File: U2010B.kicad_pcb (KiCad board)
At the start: 2 copper layers, 27 parts, among them J1 PHASE, J2 M2, J3 Rsh, J4 Rsh, J5 NULL, J6 M1, P1 50k, Q1 BT136-600, U1 U2010B

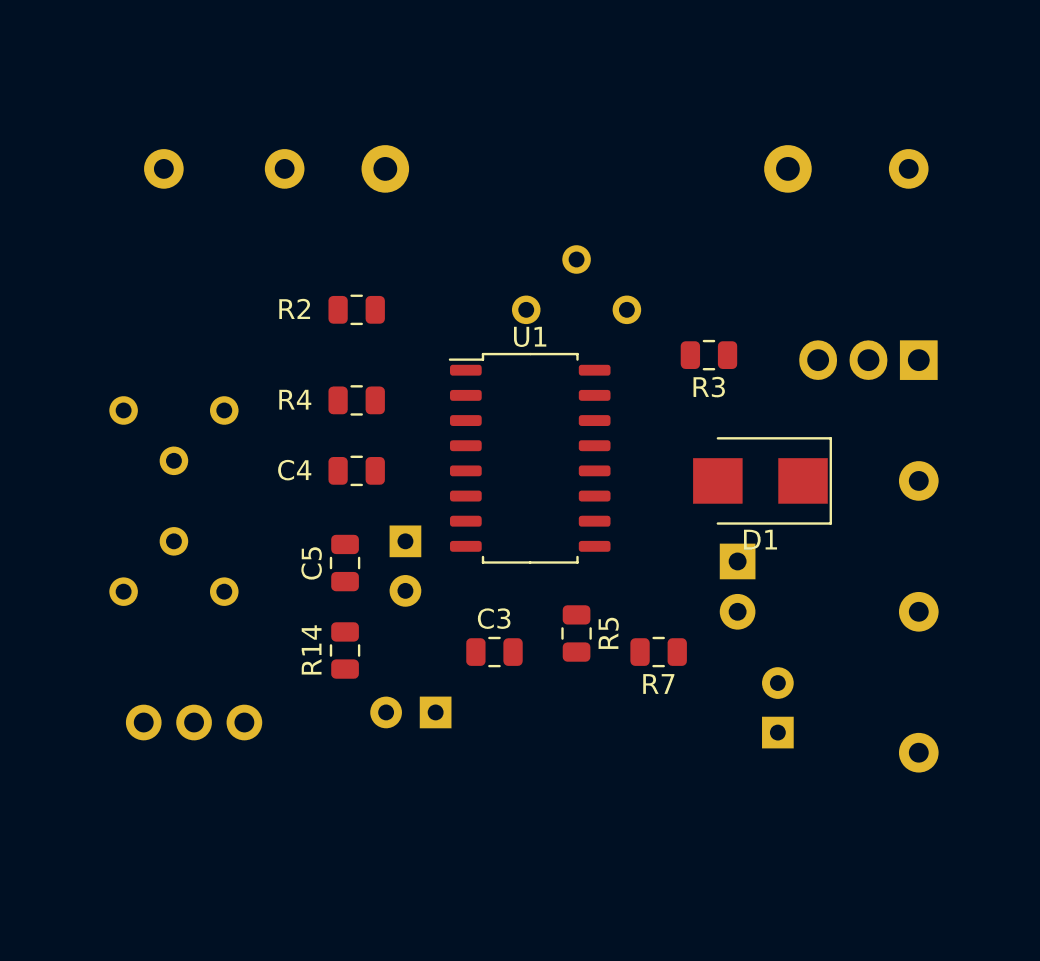
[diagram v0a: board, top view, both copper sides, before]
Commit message: Trace PCB
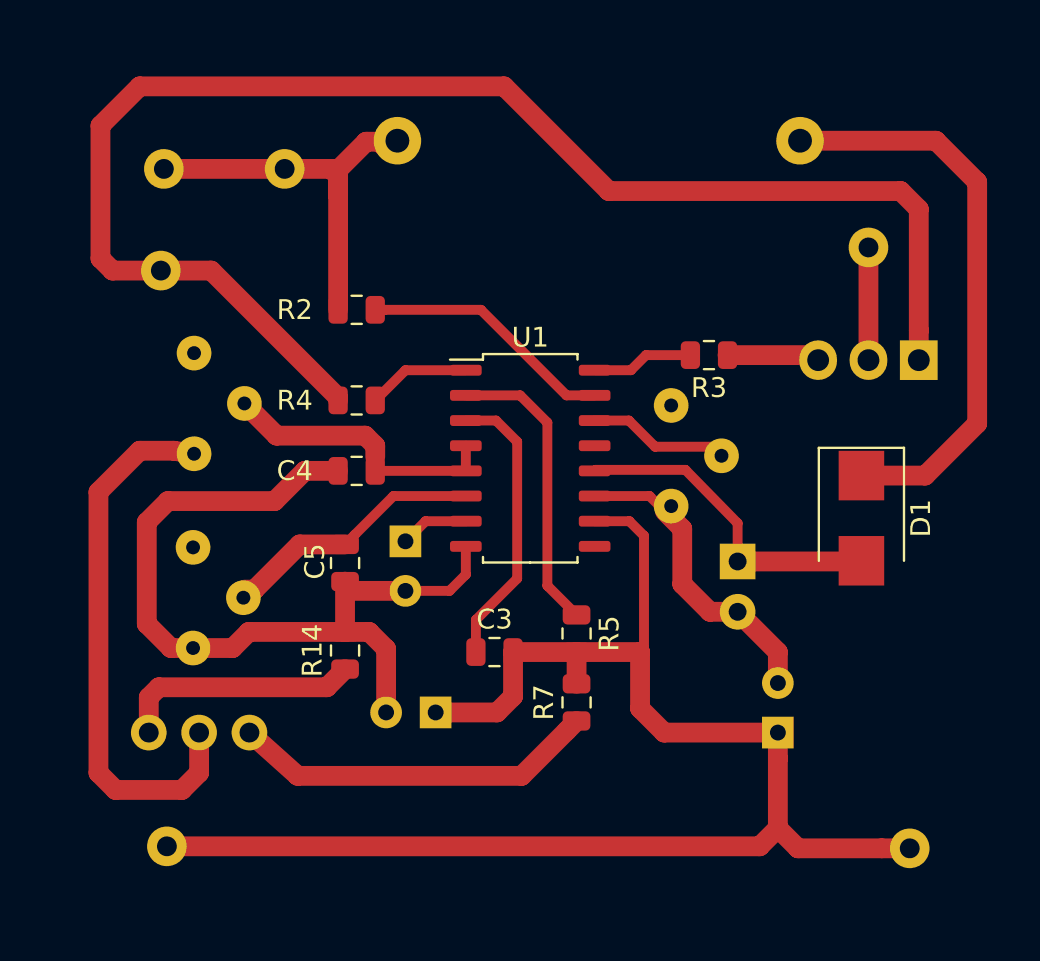
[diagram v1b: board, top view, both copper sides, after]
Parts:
- R10, R11, R8: footprint Potentiometer_THT:Potentiometer_Vishay_T7-YA_Single_Vertical -> Potentiometer_THT:Potentiometer_Bourns_3339P_Vertical_HandSoldering
- moved J3 39.7 mm to (121.3, 98.6)
- moved J4 38.2 mm to (121.6, 127.7)
- moved R8 12.3 mm to (147.0, 110.5), turned to 180 degrees
- moved J5 11.9 mm to (159.1, 127.8)
- moved D1 5.43 mm to (156.6, 111.1), turned to 270 degrees
- moved R7 4.86 mm to (142.2, 120.4), turned to 90 degrees
- moved R11 4.51 mm to (122.9, 117.7), turned to 180 degrees
- moved J6 4.45 mm to (157.0, 97.4)
- moved R10 2.66 mm to (122.9, 107.8), turned to 180 degrees
- moved R1 1.55 mm to (153.5, 92.0)
- moved P1 0.57 mm to (125.7, 121.9)
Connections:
- U1 pad 13: Net-(U1-Pad13) -> (no net)
- U1 pad 9: Net-(U1-Pad9) -> (no net)
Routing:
- net Net-(C1-Pad1): track 0.00 -> 76.7 mm
- net Net-(J3-Pad1): track 0.00 -> 74.1 mm
- net Net-(C2-Pad2): track 0.00 -> 42.2 mm
- net Net-(D1-Pad1): track 0.00 -> 28.9 mm
- net Net-(P1-Pad2): track 0.00 -> 27.7 mm
- net Net-(J1-Pad1): track 0.00 -> 20.1 mm
- net Net-(P1-Pad1): track 0.00 -> 18.5 mm
- net Net-(D1-Pad2): track 0.00 -> 16.6 mm
- net Net-(C1-Pad2): track 0.00 -> 16.1 mm
- net Net-(R5-Pad1): track 0.00 -> 15.0 mm
- net Net-(C4-Pad2): track 0.00 -> 14.6 mm
- net Net-(C3-Pad1): track 0.00 -> 14.5 mm
- net Net-(C5-Pad2): track 0.00 -> 13.1 mm
- net Net-(R2-Pad2): track 0.00 -> 12.9 mm
- net Net-(P1-Pad3): track 0.00 -> 12.3 mm
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
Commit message: Add netlist, change some pins for drill.
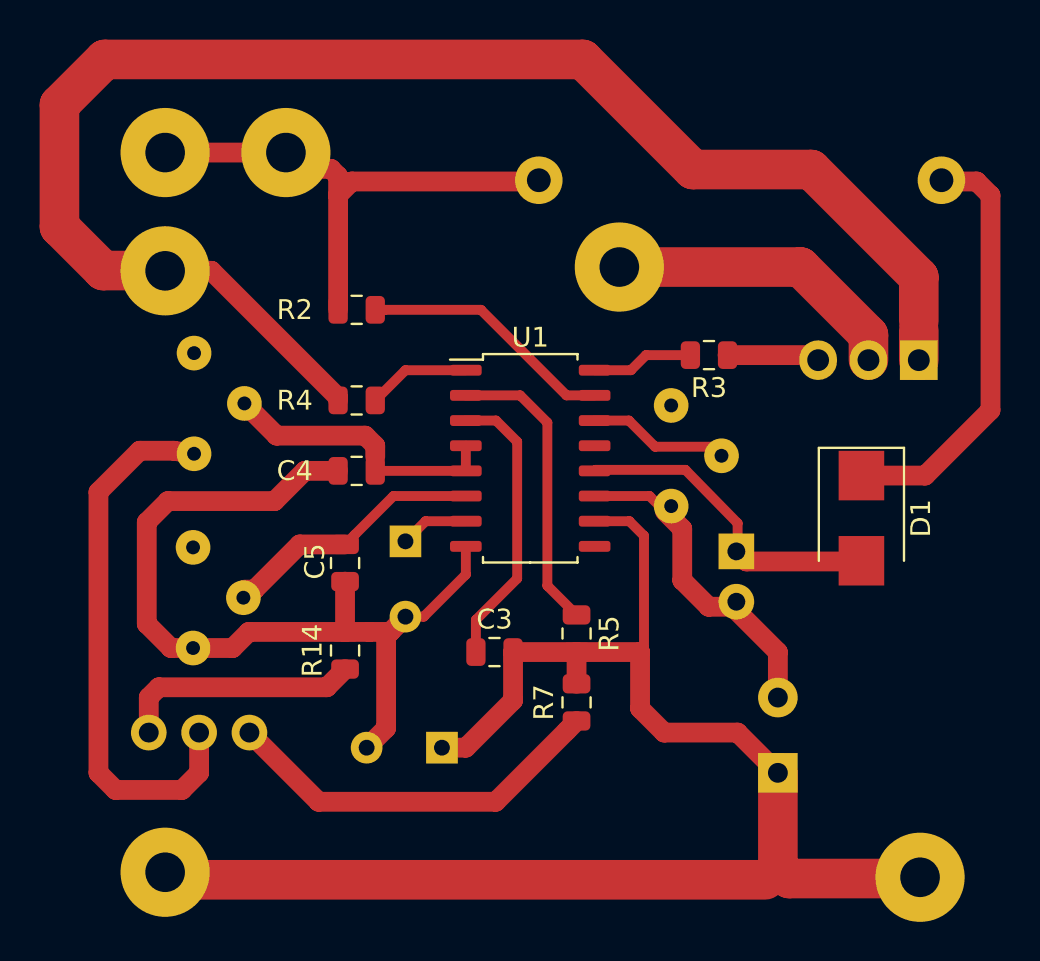
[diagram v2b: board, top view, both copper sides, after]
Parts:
- C1: footprint Capacitor_THT:CP_Radial_D6.3mm_P2.50mm -> Capacitor_THT:CP_Radial_D10.0mm_P3.80mm
- C2, C7: footprint Capacitor_THT:CP_Radial_D6.3mm_P2.50mm -> Capacitor_THT:CP_Radial_D8.0mm_P3.80mm
- D3: footprint LED_THT:LED_D3.0mm -> LED_THT:LED_D5.0mm
- J1, J2, J3, J4, J5, J6: footprint Connector_Pin:Pin_D1.0mm_L10.0mm -> Connector_Wire:SolderWirePad_1x01_Drill2mm
- moved J6 12.6 mm to (144.4, 98.4)
- moved R1 7.41 mm to (160.7, 94.0)
- moved C1 2.03 mm to (152.4, 124.0)
- moved C7 1.81 mm to (135.4, 122.7)
- moved J5 1.55 mm to (159.6, 129.2)
- moved J4 1.31 mm to (121.5, 129.0)
- moved J1 0.83 mm to (127.6, 92.6)
- moved J2 0.83 mm to (121.5, 92.6)
- moved D3 0.51 mm to (150.3, 112.8)
- moved J3 0.22 mm to (121.5, 98.6)
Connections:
- U1 pad 13: (no net) -> Net-(U1-Pad13)
- U1 pad 9: (no net) -> Net-(U1-Pad9)
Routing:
- net Net-(J6-Pad1): track 5.69 -> 15.3 mm
- net Net-(D1-Pad1): track 28.9 -> 21.5 mm
- net Net-(J1-Pad1): track 20.1 -> 26.1 mm
- net Net-(J3-Pad1): track 74.1 -> 77.0 mm
- net Net-(C2-Pad2): track 42.2 -> 43.5 mm
- net Net-(P1-Pad1): track 18.5 -> 19.6 mm
- net Net-(C1-Pad2): track 16.1 -> 16.8 mm
- net Net-(C1-Pad1): track 76.7 -> 76.1 mm
